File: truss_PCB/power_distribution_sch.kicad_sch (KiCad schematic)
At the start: 31 parts, among them IC1 BAJ0BC0FP-E2, Q8 IRF5305_PBF, U11 LM2596S-ADJ, U12 AMS1117-5.0, U13 AMS1117-3.3

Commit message: updating truss PCB
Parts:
- added J16, J17: GND, Connector_PinHeader_2.54mm:PinHeader_1x03_P2.54mm_Vertical, symbol Connector:Conn_01x03_Male
- added J18: 12V, Connector_PinHeader_2.54mm:PinHeader_1x01_P2.54mm_Vertical, symbol Connector:Conn_01x01_Male
- added J19: 6V, Connector_PinHeader_2.54mm:PinHeader_1x01_P2.54mm_Vertical, symbol Connector:Conn_01x01_Male
- added J20: 5V_MCU, Connector_PinHeader_2.54mm:PinHeader_1x01_P2.54mm_Vertical, symbol Connector:Conn_01x01_Male
- added J21: 3V3, Connector_PinHeader_2.54mm:PinHeader_1x01_P2.54mm_Vertical, symbol Connector:Conn_01x01_Male
- added J22: 10V, Connector_PinHeader_2.54mm:PinHeader_1x01_P2.54mm_Vertical, symbol Connector:Conn_01x01_Male
- renumbered C28 to EC28
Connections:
- net 10V_LC: now also R41.2, J22.1 (Pin_1); no longer D6.2 (A)
- net 12V_BUS: now also R39.2, J18.1 (Pin_1); no longer D3.2 (A)
- net 3V3_MCU: now also R43.2, J21.1 (Pin_1); no longer D8.2 (A)
- net 5V_MCU: now also R42.2, J20.1 (Pin_1); no longer D7.2 (A)
- net 6V_SERVO: now also R40.2, J19.1 (Pin_1); no longer D5.2 (A)
- net P_GND: now also D3.1 (K), D5.1 (K), D6.1 (K), D7.1 (K), D8.1 (K), J16.1 (Pin_1), J16.2 (Pin_2), J16.3 (Pin_3), J17.1 (Pin_1), J17.2 (Pin_2), J17.3 (Pin_3); no longer R39.1, R40.1, R41.1, R42.1, R43.1
- new net: D3.2 (A), R39.1
- new net: D8.2 (A), R43.1
- new net: D7.2 (A), R42.1
- new net: D5.2 (A), R40.1
- new net: D6.2 (A), R41.1

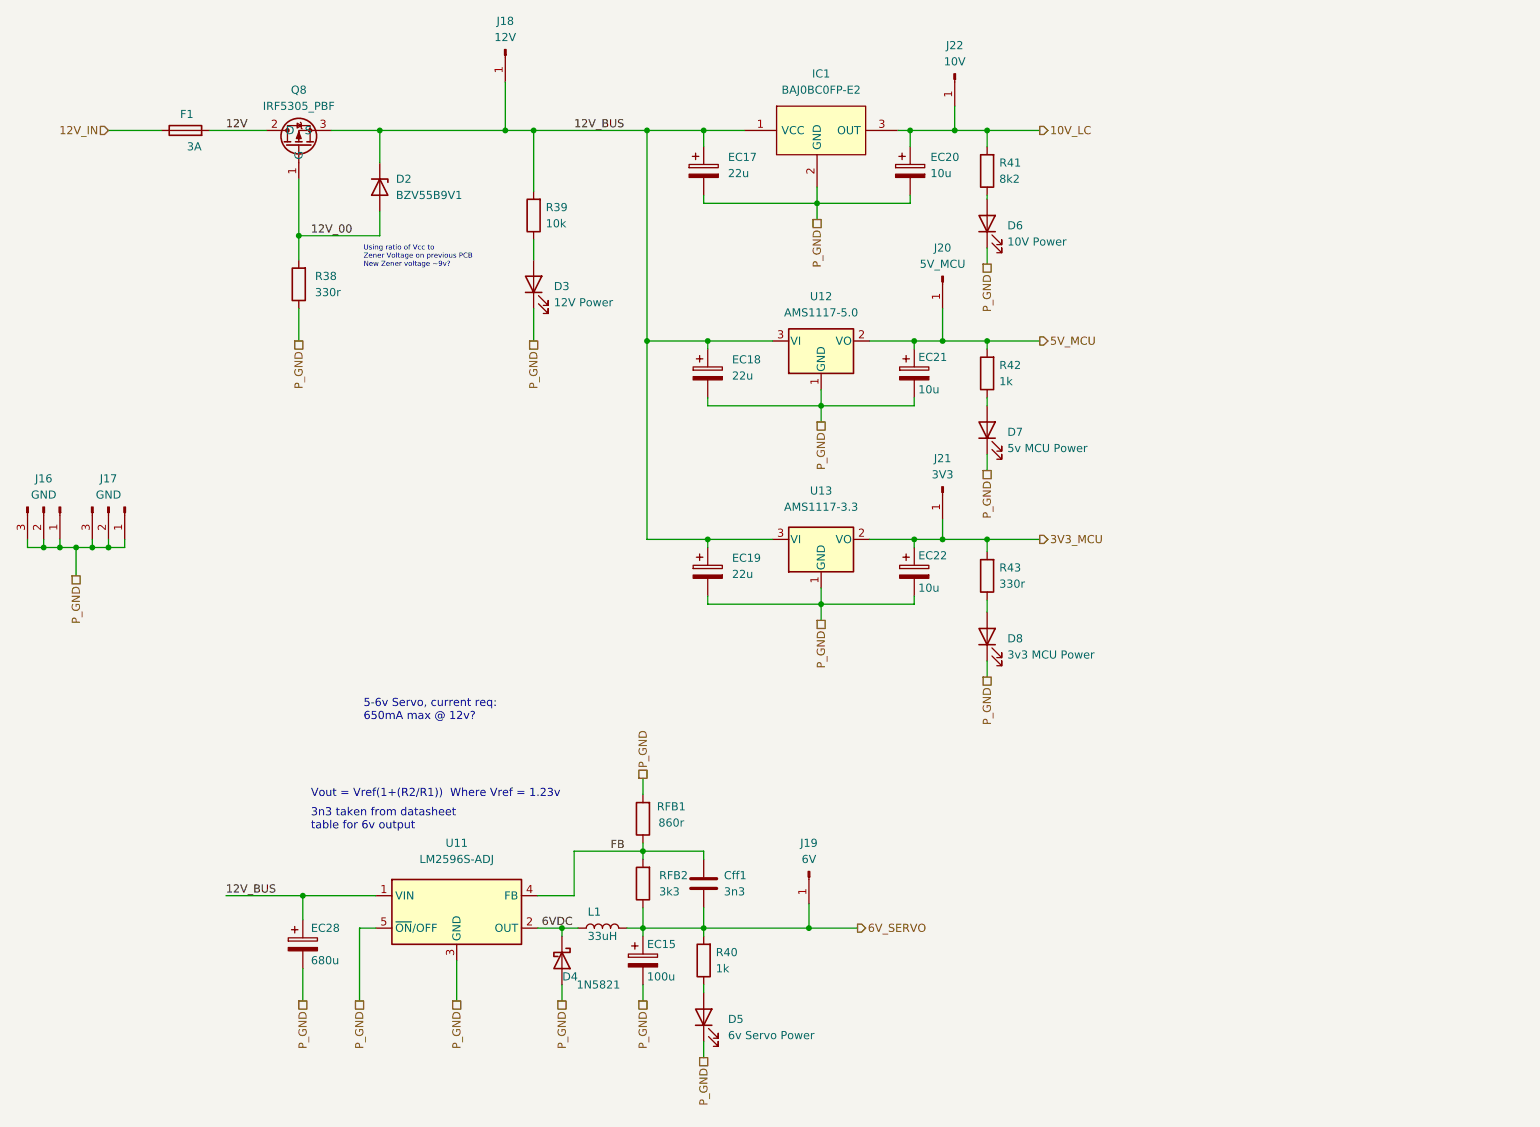
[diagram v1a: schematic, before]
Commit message: Board V2 Almost Finished TODO# RUN DRC
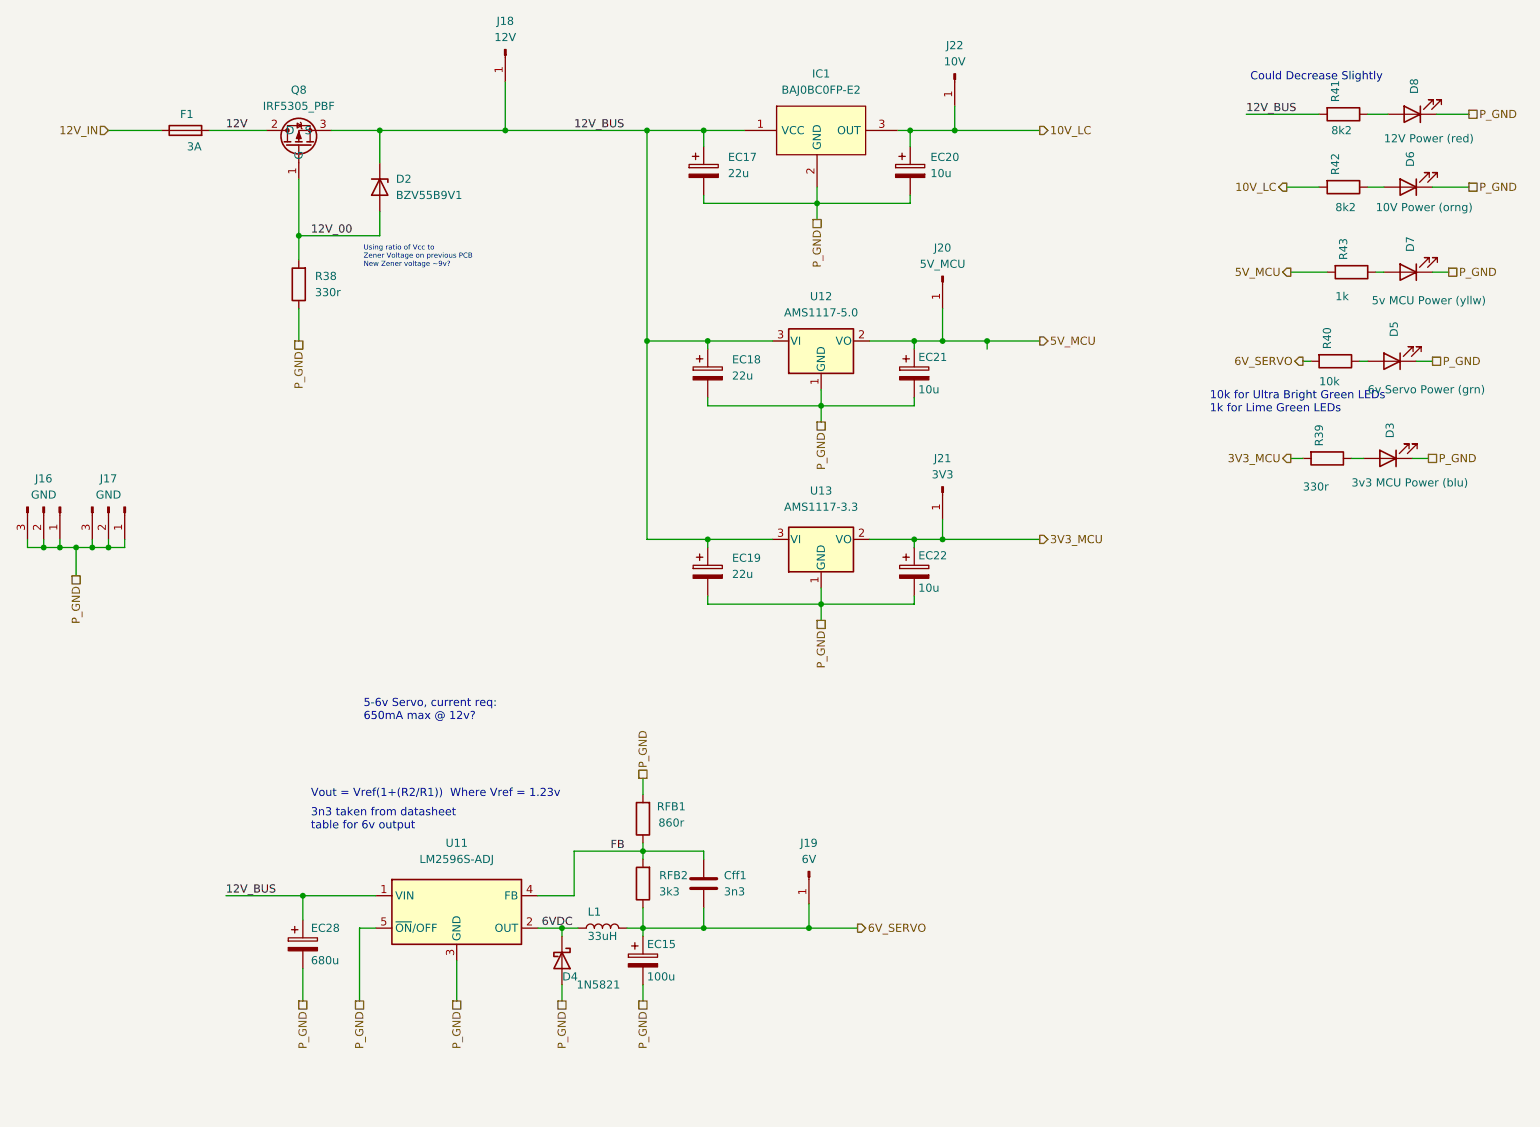
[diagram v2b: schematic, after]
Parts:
- D3: value 12V Power -> 3v3 MCU Power (blu)
- D5: value 6v Servo Power -> 6v Servo Power (grn)
- D6: value 10V Power -> 10V Power (orng)
- D7: value 5v MCU Power -> 5v MCU Power (yllw)
- D8: value 3v3 MCU Power -> 12V Power (red)
- R39: value 10k -> 330r
- R40: value 1k -> 10k
- R42: value 1k -> 8k2
- R43: value 330r -> 1k
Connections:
- net 10V_LC: now also R42.2; no longer R41.2
- net 12V_BUS: now also R41.2; no longer R39.2
- net 3V3_MCU: now also R39.2; no longer R43.2
- net 5V_MCU: now also R43.2; no longer R42.2
- net at R43.1: now also D7.2 (A); no longer D8.2 (A)
- net at R42.1: now also D6.2 (A); no longer D7.2 (A)
- net at R41.1: now also D8.2 (A); no longer D6.2 (A)
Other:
- note added: "10k for Ultra Bright Green LEDs 1k for Lime Green LEDs"
- note added: "Could Decrease Slightly"

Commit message: Finished PCB Version 2 Design
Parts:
- D3: value 3v3 MCU Power (blu) -> 3v3 MCU Power
- D5: value 6v Servo Power (grn) -> 6v Servo Power
- D6: value 10V Power (orng) -> 10V Power
- D7: value 5v MCU Power (yllw) -> 5v MCU Power
- D8: value 12V Power (red) -> 12V Power
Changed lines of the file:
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@@
       (effects (font (size 1.27 1.27)) (justify right))
     )
-    (property "Value" "3v3 MCU Power (blu)" (id 1) (at 244.475 86.36 0)
+    (property "Value" "3v3 MCU Power" (id 1) (at 244.475 86.36 0)
       (effects (font (size 1.27 1.27)) (justify right))
     )
@@
       (effects (font (size 1.27 1.27)) (justify right))
     )
-    (property "Value" "10V Power (orng)" (id 1) (at 248.285 43.18 0)
+    (property "Value" "10V Power" (id 1) (at 248.285 43.18 0)
       (effects (font (size 1.27 1.27)) (justify right))
     )
@@
       (effects (font (size 1.27 1.27)) (justify right))
     )
-    (property "Value" "6v Servo Power (grn)" (id 1) (at 247.015 71.755 0)
+    (property "Value" "6v Servo Power" (id 1) (at 247.015 71.755 0)
       (effects (font (size 1.27 1.27)) (justify right))
     )
@@
       (effects (font (size 1.27 1.27)) (justify right))
     )
-    (property "Value" "12V Power (red)" (id 1) (at 249.555 32.385 0)
+    (property "Value" "12V Power" (id 1) (at 249.555 32.385 0)
       (effects (font (size 1.27 1.27)) (justify right))
     )
@@
       (effects (font (size 1.27 1.27)) (justify right))
     )
-    (property "Value" "5v MCU Power (yllw)" (id 1) (at 247.65 57.785 0)
-      (effects (font (size 1.27 1.27)) (justify right))
-    )
+    (property "Value" "5v MCU Power" (id 1) (at 247.65 57.785 0)
+      (effects (font (size 1.27 1.27)) (justify right))
+    )
